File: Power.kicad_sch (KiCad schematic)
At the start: 11 parts

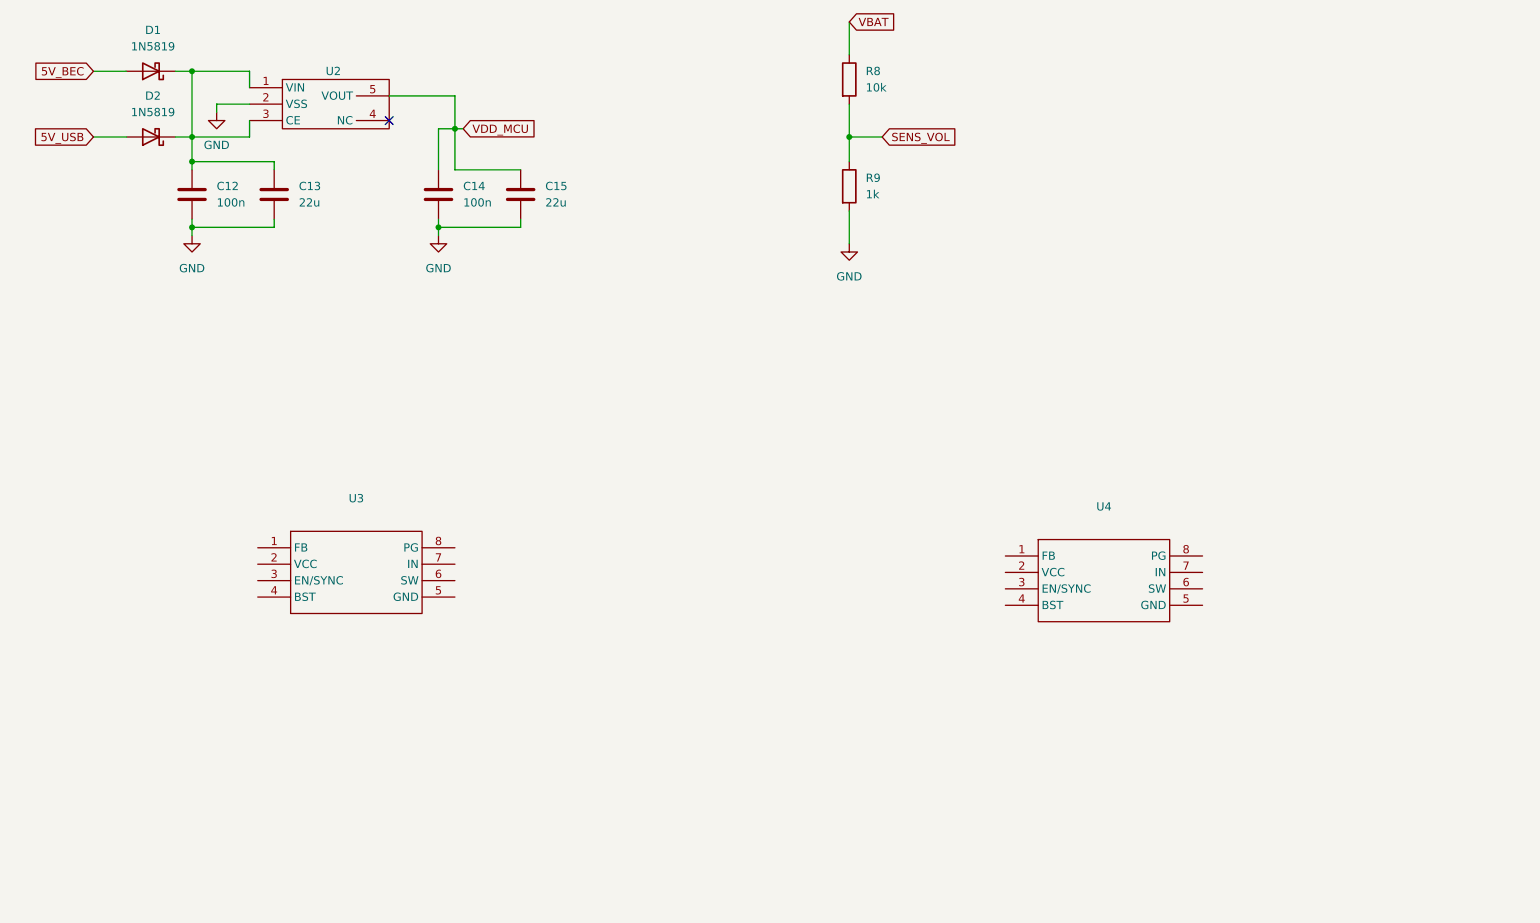
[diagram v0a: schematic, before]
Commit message: finished -power and sensors page, started OSD
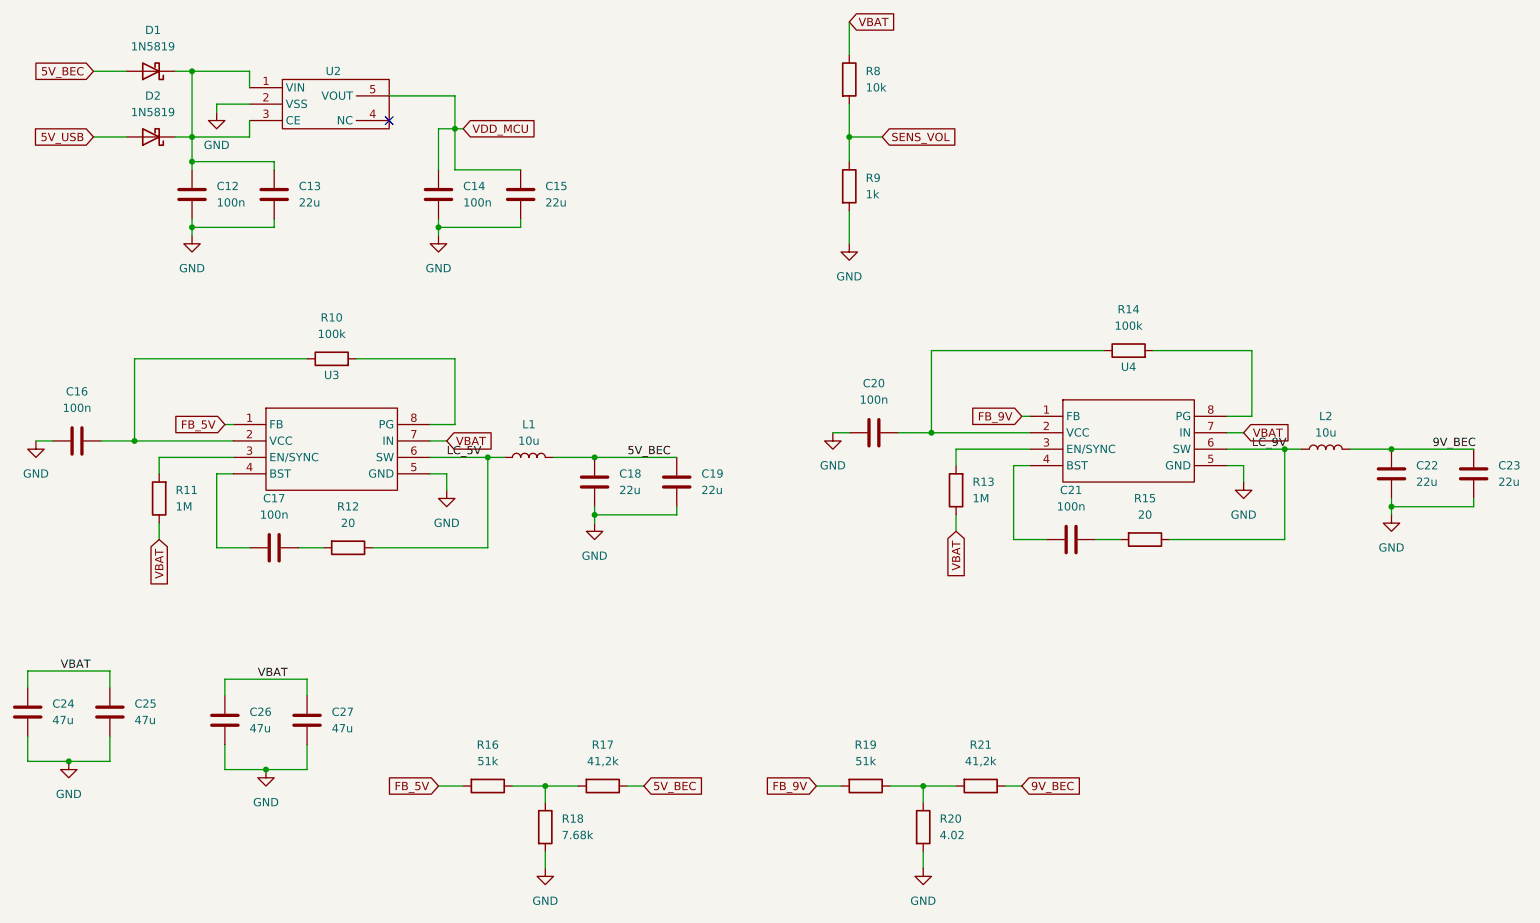
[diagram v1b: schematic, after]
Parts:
- added C16, C17, C20, C21: 100n, symbol Device:C
- added C18, C19, C22, C23: 22u, symbol Device:C
- added C24, C25, C26, C27: 47u, symbol Device:C
- added L1, L2: 10u, symbol Device:L
- added R10, R14: 100k, symbol Device:R
- added R11, R13: 1M, symbol Device:R
- added R12, R15: 20, symbol Device:R
- added R16, R19: 51k, symbol Device:R
- added R17, R21: 41,2k, symbol Device:R
- added R18: 7.68k, symbol Device:R
- added R20: 4.02, symbol Device:R
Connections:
- net 5V_BEC: now also C18.1, C19.1, L1.2, R17.1
- net GND: now also U3.5 (GND), U4.5 (GND), C16.1, C18.2, C19.2, C20.1, C22.2, C23.2, C24.2, C25.2, C26.2, C27.2, R18.2, R20.2
- net VBAT: now also U3.7 (IN), U4.7 (IN), C24.1, C25.1, C26.1, C27.1, R11.1, R13.1
- net FB_9V: now reaches U4.1 (FB)
- net FB_9V: now also R19.2
- net at U4.2 (VCC): now also C20.2, R14.1
- net at U4.3 (EN/SYNC): now also R13.2
- net at U4.4 (BST): now also C21.2
- net LC_9V: now reaches U4.6 (SW)
- net LC_9V: now also L2.1, R15.1
- net at U4.8 (PG): now also R14.2
- net FB_5V: now reaches U3.1 (FB)
- net FB_5V: now also R16.2
- net at U3.2 (VCC): now also C16.2, R10.1
- net at U3.3 (EN/SYNC): now also R11.2
- net at U3.4 (BST): now also C17.2
- net LC_5V: now reaches U3.6 (SW)
- net LC_5V: now also L1.1, R12.1
- net at U3.8 (PG): now also R10.2
- new net: R19.1, R20.1, R21.2
- new net: C21.1, R15.2
- new net: C17.1, R12.2
- new net: R16.1, R17.2, R18.1
- new net 9V_BEC: C22.1, C23.1, L2.2, R21.1
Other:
- moved on the sheet: U3

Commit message: refactor labels U and assigned resistance footprint
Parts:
- R10, R11, R12, R13, R15, R16, R18, R19, R20, R8, R9: footprint (none) -> Resistor_SMD:R_0603_1608Metric
- R14: footprint (none) -> Resistor_SMD:R_0603_1608Metric; MPN (none) -> RC0603FR-07; Manufacturer (none) -> Yageo
- R17, R21: value 41,2k -> 41.2k; footprint (none) -> Resistor_SMD:R_0603_1608Metric
- U1: renamed from U2; value ~ -> ME6217C33M5G
- U2: renamed from U4; value ~ -> MP9943GQ-Z
- U3: value ~ -> MP9943GQ-Z
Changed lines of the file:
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@@
 			)
 		)
-		(property "Footprint" ""
+		(property "Footprint" "Resistor_SMD:R_0603_1608Metric"
 			(at 168.402 149.86 90)
 			(effects
@@
 	)
 	(symbol
+		(lib_name "MP9943GQ-z_1")
 		(lib_id "fclib:MP9943GQ-z")
-		(at 189.23 81.28 0)
-		(unit 1)
-		(exclude_from_sim no)
-		(in_bom yes)
-		(on_board yes)
-		(dnp no)
-		(fields_autoplaced yes)
-		(property "Reference" "U4"
-			(at 201.93 78.74 0)
-			(effects
-				(font
-					(size 1.27 1.27)
-				)
-			)
-		)
-		(property "Value" "~"
-			(at 201.93 81.28 0)
+		(at 201.93 90.17 0)
+		(unit 1)
+		(exclude_from_sim no)
+		(in_bom yes)
+		(on_board yes)
+		(dnp no)
+		(property "Reference" "U2"
+			(at 194.056 82.804 0)
+			(effects
+				(font
+					(size 1.27 1.27)
+				)
+			)
+		)
+		(property "Value" "MP9943GQ-Z"
+			(at 209.042 82.804 0)
 			(effects
 				(font
@@
 		)
 		(property "Footprint" ""
-			(at 189.23 81.28 0)
+			(at 201.93 90.17 0)
 			(effects
 				(font
@@
 		)
 		(property "Datasheet" ""
-			(at 189.23 81.28 0)
+			(at 201.93 90.17 0)
 			(effects
 				(font
@@
 		)
 		(property "Description" ""
-			(at 189.23 81.28 0)
+			(at 201.93 90.17 0)
 			(effects
 				(font
@@
 			(project "fch7"
 				(path "/11716af6-0e6e-444b-b738-3f12da23c1a2/436f6237-706d-4072-be43-3abf579550aa"
-					(reference "U4")
+					(reference "U2")
 					(unit 1)
 				)
@@
 			)
 		)
-		(property "Footprint" ""
+		(property "Footprint" "Resistor_SMD:R_0603_1608Metric"
 			(at 201.93 77.978 90)
 			(effects
@@
 			)
 		)
+		(property "Manufacturer" "Yageo"
+			(at 201.93 76.2 90)
+			(effects
+				(font
+					(size 1.27 1.27)
+				)
+				(hide yes)
+			)
+		)
+		(property "MPN" "RC0603FR-07"
+			(at 201.93 76.2 90)
+			(effects
+				(font
+					(size 1.27 1.27)
+				)
+				(hide yes)
+			)
+		)
+		(property "Field7" ""
+			(at 201.93 76.2 90)
+			(effects
+				(font
+					(size 1.27 1.27)
+				)
+				(hide yes)
+			)
+		)
+		(property "Field8" ""
+			(at 201.93 76.2 90)
+			(effects
+				(font
+					(size 1.27 1.27)
+				)
+				(hide yes)
+			)
+		)
 		(pin "2"
 		)
@@
 			)
 		)
-		(property "Footprint" ""
+		(property "Footprint" "Resistor_SMD:R_0603_1608Metric"
 			(at 204.47 103.632 90)
 			(effects
@@
 			)
 		)
-		(property "Value" "41,2k"
+		(property "Value" "41.2k"
 			(at 179.07 139.7 90)
 			(effects
@@
 			)
 		)
-		(property "Footprint" ""
+		(property "Footprint" "Resistor_SMD:R_0603_1608Metric"
 			(at 179.07 141.732 90)
 			(effects
@@
 			)
 		)
-		(property "Footprint" ""
+		(property "Footprint" "Resistor_SMD:R_0603_1608Metric"
 			(at 81.28 104.902 90)
 			(effects
@@
 			)
 		)
-		(property "Footprint" ""
+		(property "Footprint" "Resistor_SMD:R_0603_1608Metric"
 			(at 78.74 79.248 90)
 			(effects
@@
 			)
 		)
-		(property "Footprint" ""
+		(property "Footprint" "Resistor_SMD:R_0603_1608Metric"
 			(at 161.29 141.732 90)
 			(effects
@@
 			)
 		)
-		(property "Value" "41,2k"
+		(property "Value" "41.2k"
 			(at 120.65 139.7 90)
 			(effects
@@
 			)
 		)
-		(property "Footprint" ""
+		(property "Footprint" "Resistor_SMD:R_0603_1608Metric"
 			(at 120.65 141.732 90)
 			(effects
@@
 			)
 		)
-		(property "Footprint" ""
+		(property "Footprint" "Resistor_SMD:R_0603_1608Metric"
 			(at 53.848 99.06 90)
 			(effects
@@
 			)
 		)
-		(property "Footprint" ""
+		(property "Footprint" "Resistor_SMD:R_0603_1608Metric"
 			(at 109.982 149.86 90)
 			(effects
@@
 	(symbol
 		(lib_id "fclib:ME6217c33M5G")
-		(at 67.31 31.75 0)
-		(unit 1)
-		(exclude_from_sim no)
-		(in_bom yes)
-		(on_board yes)
-		(dnp no)
-		(property "Reference" "U2"
+		(at 78.74 38.1 0)
+		(unit 1)
+		(exclude_from_sim no)
+		(in_bom yes)
+		(on_board yes)
+		(dnp no)
+		(property "Reference" "U1"
 			(at 78.994 33.02 0)
 			(effects
@@
 			)
 		)
-		(property "Value" "~"
-			(at 79.375 31.75 0)
-			(effects
-				(font
-					(size 1.27 1.27)
-				)
-				(hide yes)
+		(property "Value" "ME6217C33M5G"
+			(at 79.248 43.18 0)
+			(effects
+				(font
+					(size 1.27 1.27)
+				)
 			)
 		)
 		(property "Footprint" ""
-			(at 67.31 31.75 0)
+			(at 78.74 38.1 0)
 			(effects
 				(font
@@
 		)
 		(property "Datasheet" ""
-			(at 67.31 31.75 0)
+			(at 78.74 38.1 0)
 			(effects
 				(font
@@
 		)
 		(property "Description" ""
-			(at 67.31 31.75 0)
+			(at 78.74 38.1 0)
+			(effects
+				(font
+					(size 1.27 1.27)
+				)
+				(hide yes)
+			)
+		)
+		(property "MPN" ""
+			(at 78.74 38.1 0)
 			(effects
 				(font
@@
 			(project ""
 				(path "/11716af6-0e6e-444b-b738-3f12da23c1a2/436f6237-706d-4072-be43-3abf579550aa"
-					(reference "U2")
+					(reference "U1")
 					(unit 1)
 				)
@@
 			)
 		)
-		(property "Footprint" ""
+		(property "Footprint" "Resistor_SMD:R_0603_1608Metric"
 			(at 156.972 34.29 90)
 			(effects
@@
 	(symbol
 		(lib_id "fclib:MP9943GQ-z")
-		(at 66.04 82.55 0)
-		(unit 1)
-		(exclude_from_sim no)
-		(in_bom yes)
-		(on_board yes)
-		(dnp no)
-		(fields_autoplaced yes)
+		(at 78.74 91.44 0)
+		(unit 1)
+		(exclude_from_sim no)
+		(in_bom yes)
+		(on_board yes)
+		(dnp no)
 		(property "Reference" "U3"
-			(at 78.74 80.01 0)
-			(effects
-				(font
-					(size 1.27 1.27)
-				)
-			)
-		)
-		(property "Value" "~"
-			(at 78.74 82.55 0)
+			(at 70.866 84.328 0)
+			(effects
+				(font
+					(size 1.27 1.27)
+				)
+			)
+		)
+		(property "Value" "MP9943GQ-Z"
+			(at 87.884 84.328 0)
 			(effects
 				(font
@@
 		)
 		(property "Footprint" ""
-			(at 66.04 82.55 0)
+			(at 78.74 91.44 0)
 			(effects
 				(font
@@
 		)
 		(property "Datasheet" ""
-			(at 66.04 82.55 0)
+			(at 78.74 91.44 0)
 			(effects
 				(font
@@
 		)
 		(property "Description" ""
-			(at 66.04 82.55 0)
+			(at 78.74 91.44 0)
 			(effects
 				(font
@@
 			)
 		)
-		(property "Footprint" ""
+		(property "Footprint" "Resistor_SMD:R_0603_1608Metric"
 			(at 102.87 141.732 90)
 			(effects
@@
 			)
 		)
-		(property "Footprint" ""
+		(property "Footprint" "Resistor_SMD:R_0603_1608Metric"
 			(at 156.972 50.8 90)
 			(effects
@@
 			)
 		)
-		(property "Footprint" ""
+		(property "Footprint" "Resistor_SMD:R_0603_1608Metric"
 			(at 177.038 97.79 90)
 			(effects

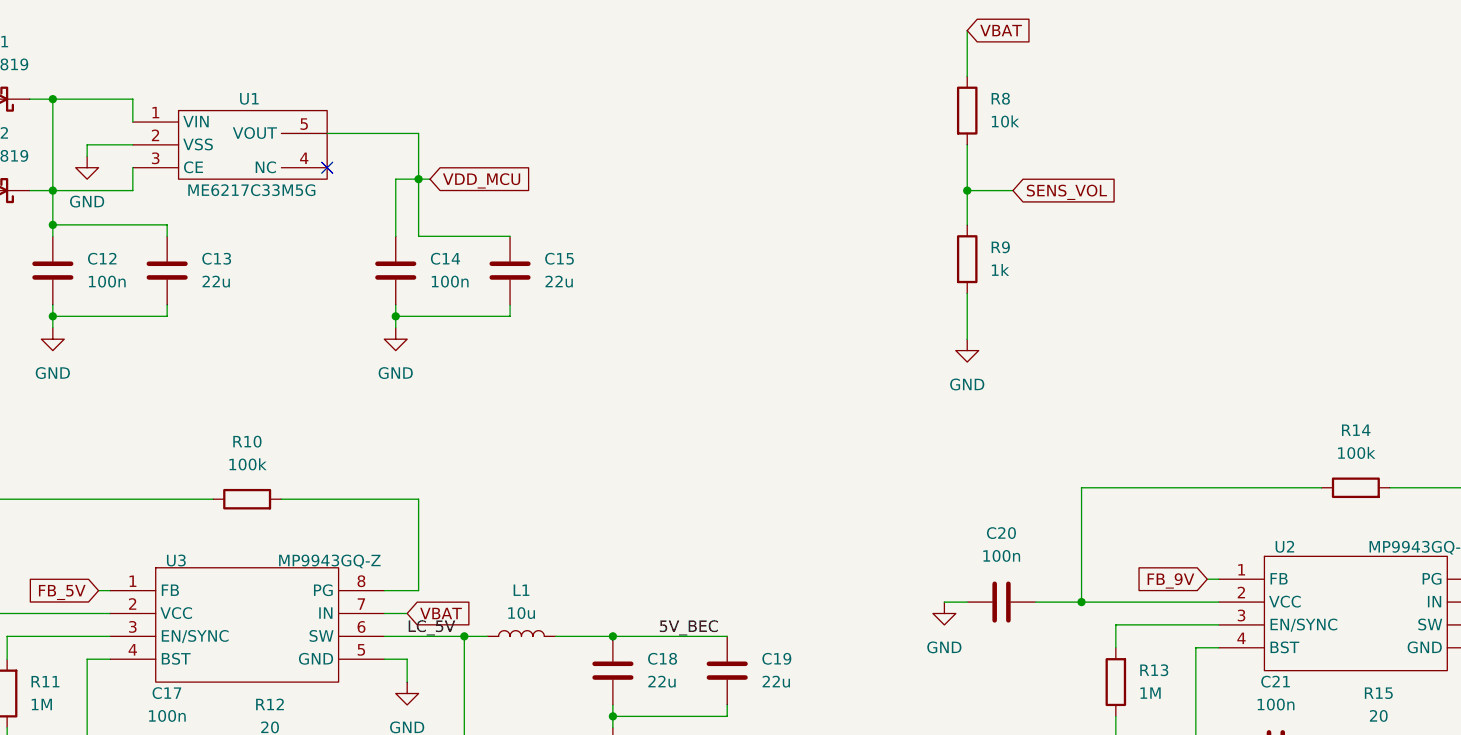
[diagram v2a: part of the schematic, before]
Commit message: refactor and update references, added some footprints
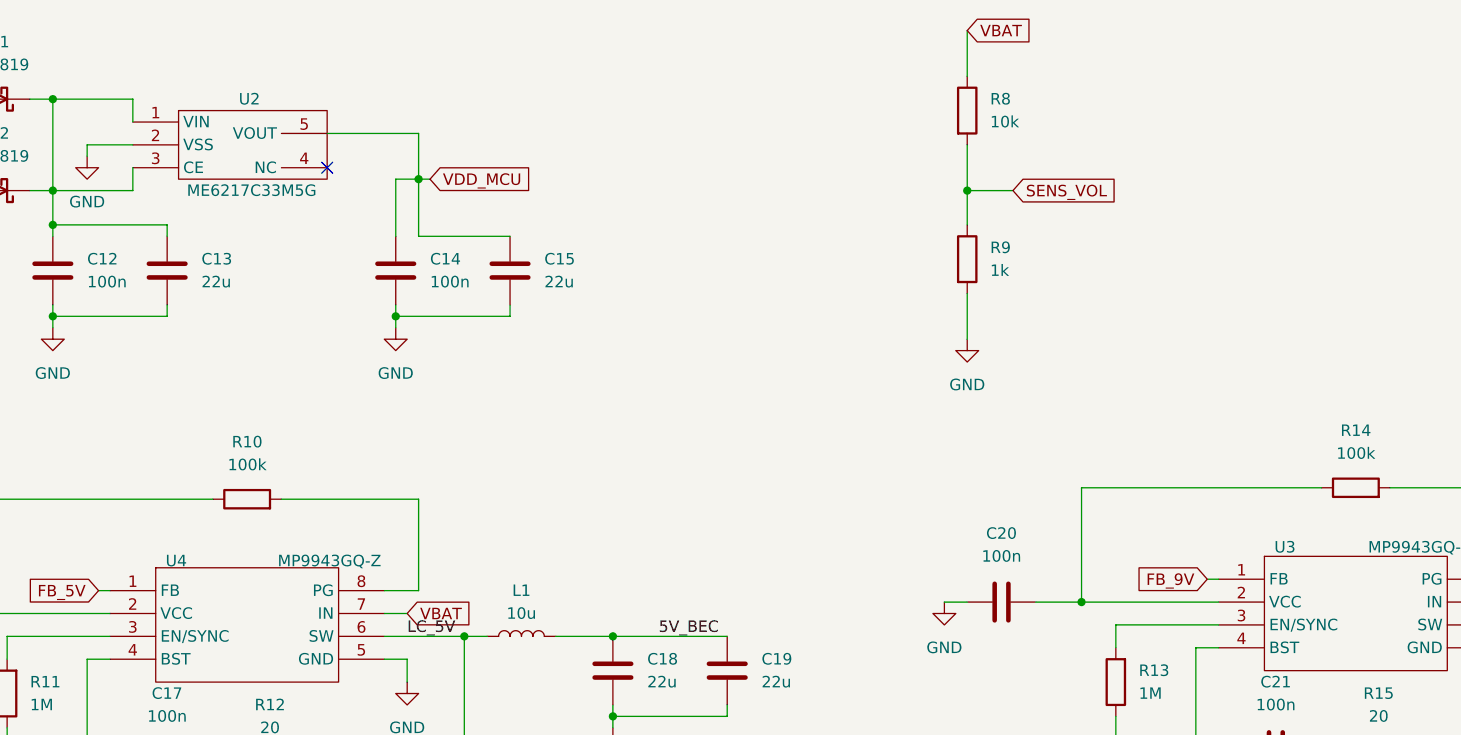
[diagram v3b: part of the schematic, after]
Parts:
- C12, C14, C16, C17, C20, C21: footprint (none) -> Capacitor_SMD:C_0603_1608Metric
- C13, C15, C18, C19, C22, C23, C24, C25, C26, C27: footprint (none) -> Capacitor_SMD:C_1210_3225Metric
- L1, L2: footprint (none) -> Inductor_SMD:L_0805_2012Metric
- R14: MPN RC0603FR-07 -> (none)
- renumbered U1 to U2, U2 to U3, U3 to U4
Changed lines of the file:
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@@
 		(on_board yes)
 		(dnp no)
-		(property "Reference" "U2"
+		(property "Reference" "U3"
 			(at 194.056 82.804 0)
 			(effects
@@
 			(project "fch7"
 				(path "/11716af6-0e6e-444b-b738-3f12da23c1a2/436f6237-706d-4072-be43-3abf579550aa"
-					(reference "U2")
+					(reference "U3")
 					(unit 1)
 				)
@@
 			)
 		)
-		(property "Footprint" ""
+		(property "Footprint" "Capacitor_SMD:C_1210_3225Metric"
 			(at 75.8952 137.16 0)
 			(effects
@@
 			)
 		)
-		(property "Footprint" ""
+		(property "Footprint" "Capacitor_SMD:C_1210_3225Metric"
 			(at 63.1952 137.16 0)
 			(effects
@@
 			)
 		)
-		(property "Footprint" ""
+		(property "Footprint" "Capacitor_SMD:C_1210_3225Metric"
 			(at 120.3452 100.33 0)
 			(effects
@@
 			)
 		)
-		(property "Footprint" ""
+		(property "Footprint" "Capacitor_SMD:C_0603_1608Metric"
 			(at 96.2152 55.88 0)
 			(effects
@@
 			)
 		)
-		(property "MPN" "RC0603FR-07"
+		(property "MPN" ""
 			(at 201.93 76.2 90)
 			(effects
@@
 			)
 		)
-		(property "Footprint" ""
+		(property "Footprint" "Capacitor_SMD:C_0603_1608Metric"
 			(at 189.23 106.3752 0)
 			(effects
@@
 			)
 		)
-		(property "Footprint" ""
+		(property "Footprint" "Capacitor_SMD:C_0603_1608Metric"
 			(at 58.1152 55.88 0)
 			(effects
@@
 			)
 		)
-		(property "Footprint" ""
+		(property "Footprint" "Capacitor_SMD:C_0603_1608Metric"
 			(at 166.37 87.9348 0)
 			(effects
@@
 			)
 		)
-		(property "Footprint" ""
+		(property "Footprint" "Capacitor_SMD:C_1210_3225Metric"
 			(at 256.2352 99.06 0)
 			(effects
@@
 			)
 		)
-		(property "Footprint" ""
+		(property "Footprint" "Capacitor_SMD:C_1210_3225Metric"
 			(at 70.8152 55.88 0)
 			(effects
@@
 			)
 		)
-		(property "Footprint" ""
+		(property "Footprint" "Capacitor_SMD:C_1210_3225Metric"
 			(at 108.9152 55.88 0)
 			(effects
@@
 			)
 		)
-		(property "Footprint" ""
+		(property "Footprint" "Capacitor_SMD:C_1210_3225Metric"
 			(at 45.4152 135.89 0)
 			(effects
@@
 		(on_board yes)
 		(dnp no)
-		(property "Reference" "U1"
+		(property "Reference" "U2"
 			(at 78.994 33.02 0)
 			(effects
@@
 			(project ""
 				(path "/11716af6-0e6e-444b-b738-3f12da23c1a2/436f6237-706d-4072-be43-3abf579550aa"
-					(reference "U1")
+					(reference "U2")
 					(unit 1)
 				)
@@
 			)
 		)
-		(property "Footprint" ""
+		(property "Footprint" "Capacitor_SMD:C_0603_1608Metric"
 			(at 66.04 107.6452 0)
 			(effects
@@
 		(on_board yes)
 		(dnp no)
-		(property "Reference" "U3"
+		(property "Reference" "U4"
 			(at 70.866 84.328 0)
 			(effects
@@
 			(project ""
 				(path "/11716af6-0e6e-444b-b738-3f12da23c1a2/436f6237-706d-4072-be43-3abf579550aa"
-					(reference "U3")
+					(reference "U4")
 					(unit 1)
 				)
@@
 			)
 		)
-		(property "Footprint" ""
+		(property "Footprint" "Inductor_SMD:L_0805_2012Metric"
 			(at 109.22 92.71 0)
 			(effects
@@
 			)
 		)
-		(property "Footprint" ""
+		(property "Footprint" "Capacitor_SMD:C_1210_3225Metric"
 			(at 133.0452 100.33 0)
 			(effects
@@
 			)
 		)
-		(property "Footprint" ""
+		(property "Footprint" "Capacitor_SMD:C_1210_3225Metric"
 			(at 243.5352 99.06 0)
 			(effects
@@
 			)
 		)
-		(property "Footprint" ""
+		(property "Footprint" "Capacitor_SMD:C_0603_1608Metric"
 			(at 43.18 89.2048 0)
 			(effects
@@
 			)
 		)
-		(property "Footprint" ""
+		(property "Footprint" "Capacitor_SMD:C_1210_3225Metric"
 			(at 32.7152 135.89 0)
 			(effects
@@
 			)
 		)
-		(property "Footprint" ""
+		(property "Footprint" "Inductor_SMD:L_0805_2012Metric"
 			(at 232.41 91.44 0)
 			(effects
